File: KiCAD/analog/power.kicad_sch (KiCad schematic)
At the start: 31 parts, among them J33 Screw_Terminal_01x02, J34 Screw_Terminal_01x02, J5 Screw_Terminal_01x02, K5 G6RL-1-DC12, U13 MCP1700x-330xxTO, U6 LM2940CT-5.0, U7 LT1054, U8 LM2940CT-12, U9 LT1054

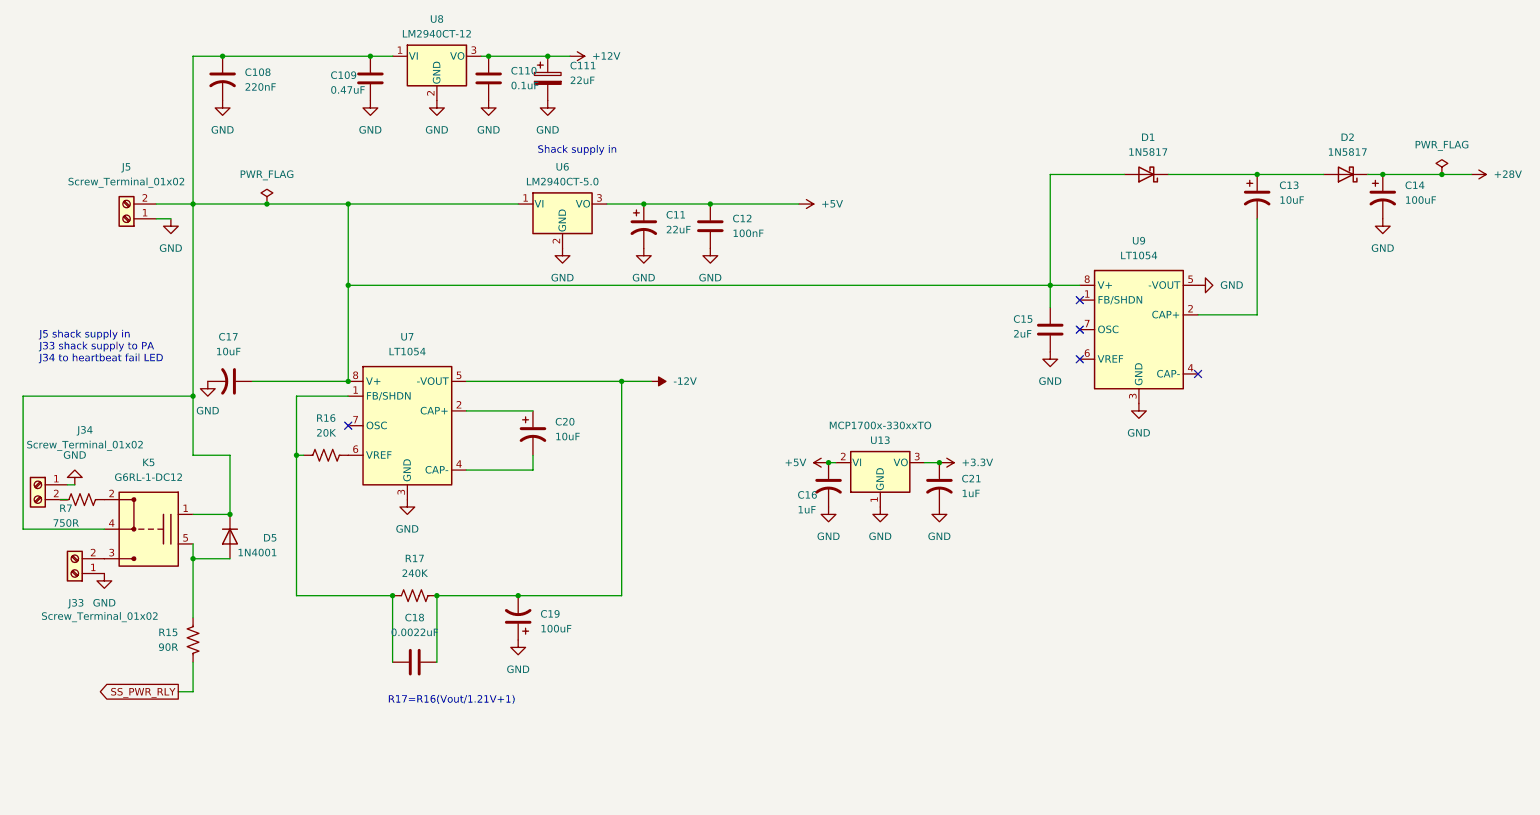
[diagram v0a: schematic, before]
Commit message: revD: drop 10m, convert LPF to DPDT G6K throughout, retire +28V rail
Output LPF:
- 10m bank removed (K8/K1-equivalent, L15/L16/L17, CF14-CF25 and
  parallel-cap combos, R4 original). 10m to be handled via main rig.
- All 4 remaining bands now use a single xmitter:Relay_G6K DPDT per
  bank (K1=15m, K2=17m, K3=20m, K4=40m). Pole 1 switches output,
  Pole 2 switches input. Half the relay count vs the old SPST pair.
- Coil chain per bank: pin1=+12V, pin8=RLY_xx_DRIVE via 2N7000
  (Q5/Q8/Q1/Q10 for 15/17/20/40) with 1N4148 flyback (D7/D8/D9/D11).
- Swamp resistors (R2-R9, 2 per bank) placed on relay pin 7 (NC) so
  they only load the LPF when the bank is unselected -- removes
  active-path insertion loss.
- Legacy screw terminals J16/J25/J26/J27/J29 and +28V coil feed
  deleted. Umbilical now carries +12V on J2 pin 8.

Analog:
- LT1054 +28V voltage doubler (U9) and its support caps/diodes
  removed. +28V net purged from every sheet.
- +12V (LM2940CT-12 U8) now feeds the LPF coil supply via J2 pin 8.
- LT1054 -12V inverter (U7) retained for LM7171 negative rail.
- +12V current budget: ~75-100 mA worst case (op-amp rails + one
  G6K coil active) against 1 A LDO capacity.

Co-Authored-By: Claude Opus 4.7 <noreply@anthropic.com>
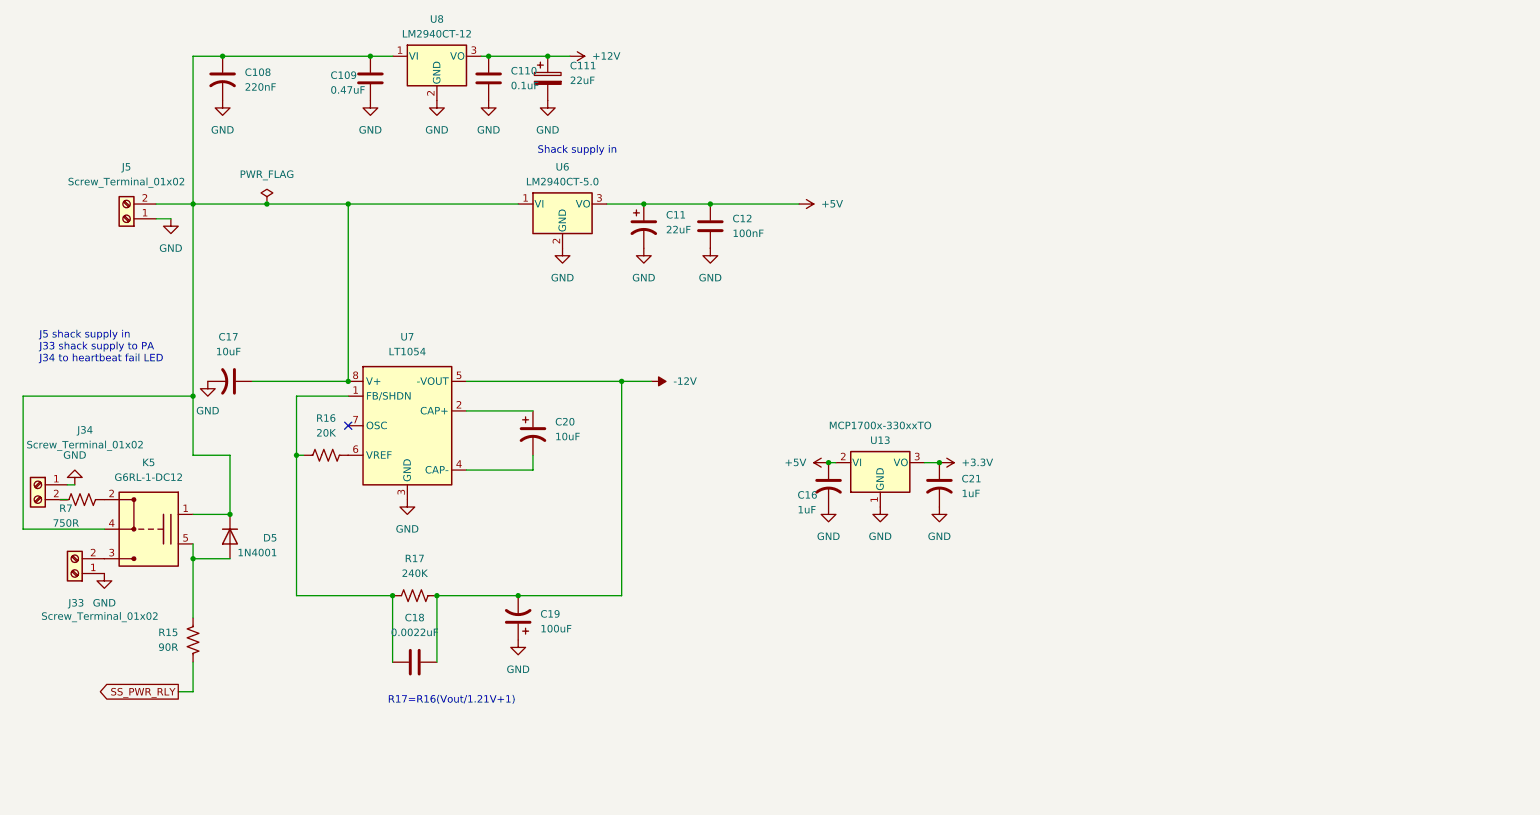
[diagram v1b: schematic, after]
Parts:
- removed C13: 10uF, Capacitor_THT:CP_Radial_D5.0mm_P2.00mm, symbol Device:C_Polarized_US
- removed C14: 100uF, Capacitor_THT:CP_Radial_D8.0mm_P5.00mm, symbol Device:C_Polarized_US
- removed C15: 2uF, Capacitor_THT:C_Rect_L7.2mm_W4.5mm_P5.00mm, symbol Device:C
- removed D1, D2: 1N5817, Diode_THT:D_DO-41_SOD81_P10.16mm_Horizontal, symbol Diode:1N5817
- removed U9: LT1054, Package_DIP:DIP-8_W7.62mm, symbol Regulator_SwitchedCapacitor:LT1054
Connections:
- no-connect marks 5 -> 1

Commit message: revD analog: shack supply input protection -- fuse + Schottky
- Add 3A slow-blow blade fuse on +13.8V input at J5. Catches
  downstream shorts (IRF510 drain-source failure, trace short)
  before the drain-feed trace, T203 bifilar, or shack-supply wiring
  smokes. Blows well below the shack supply's own ~25A protection.
- Add reverse-polarity Schottky in series on the input path (1N5822
  or SB540 class).
- xmitter library additions:
    * symbol:   Fuse_Blade_3568 (copied from stock Device:Fuse,
                pre-linked to the footprint below, default value
                Fuse_3A_SlowBlow)
    * footprint: Fuse_Blade_Keystone_3568 (Keystone 3568 PCB-mount
                 ATM mini blade fuse holder; 16 x 6.73 mm body, 4
                 x 1.6 mm NPTH on 9.92 x 3.40 mm 2x2 pattern)
- Documentation: Keystone 3568 datasheet (3568 holder.pdf)

Co-Authored-By: Claude Opus 4.7 <noreply@anthropic.com>
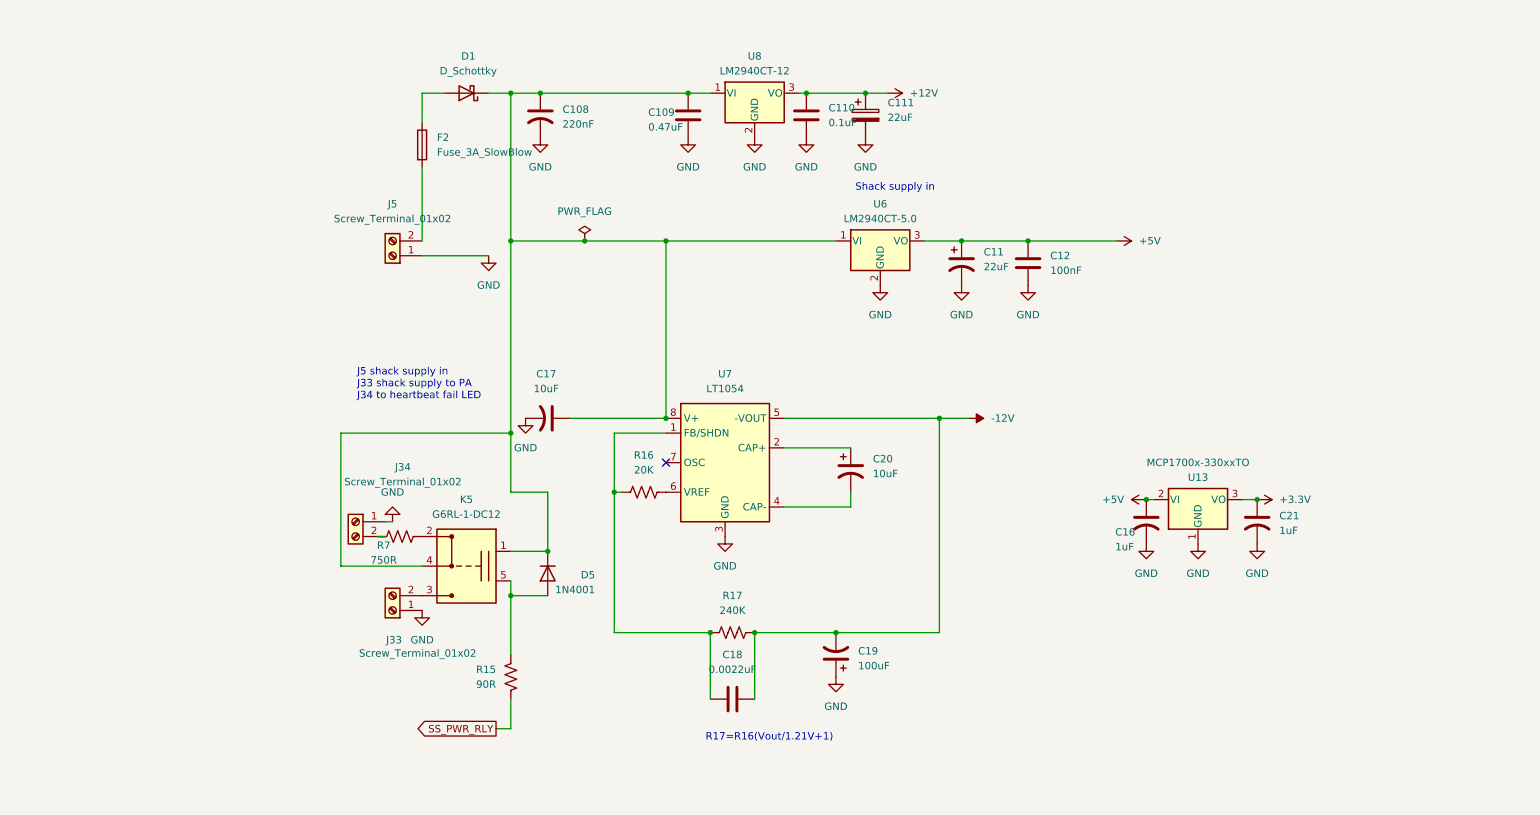
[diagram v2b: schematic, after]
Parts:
- added D1: D_Schottky, symbol Device:D_Schottky
- added F2: Fuse_3A_SlowBlow, xmitter:Fuse_Blade_Keystone_3568, symbol xmitter:Fuse_Blade_3568
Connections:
- net at C108.1, C109.1, C17.1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: now also D1.1 (K); no longer J5.2 (Pin_2)
- new net: D1.2 (A), F2.1
- new net: F2.2, J5.2 (Pin_2)
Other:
- moved on the sheet: C108, C109, C11, C110, C111, C12, C16, C17, C18, C19, C20, C21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

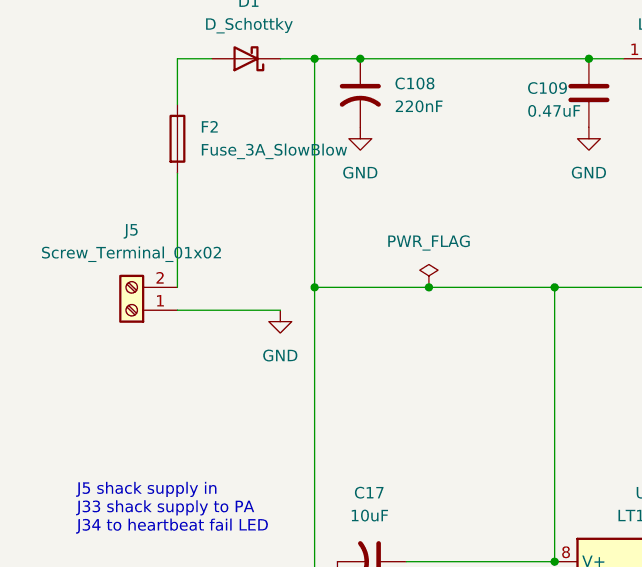
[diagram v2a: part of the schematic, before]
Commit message: revD: ss_pa Option C 5V rail + analog SW1 THT + R/C footprints + doc refresh
ss_pa Option C: swap U13 to LM2936Z-5.0 (full +5V logic rail), re-size
R10 10K->6.8K to preserve ~0.3V fault trip at new rail, drop +3.3V net
entirely. Fixes the previously-dead +5V bus that had no source.

Analog SW1 (Si5351 bringup DPDT): swap SMD footprint for
Button_Switch_THT:SW_CK_JS202011CQN_DPDT_Straight. Verified pin-numbering
convention (pin 1 above pin 6 in THT) matches user's intended DPST
wiring; both SDA/SCL break together.

Analog: assign missing footprints to R3/R4/R5/R8/R9 (DIN0207 axial) and
C4/C5/C6/C7/C8 (disc ceramic 5mm). Add xmitter:DIP-14_W7.62mm.kicad_mod
and 74HCT125 symbol to the xmitter library.

Documentation: Rev D handoff doc updated with M1-M8 fix status, Option C
notes, I2C bus voltage architecture, 74HCT125 SPI shifter, FAULT_N
divider details, and Metro-no-footprint note. Supporting docs updated:
i2c_bus.md full rewrite for 5V HV bus + STEMMA reroute, revD_interconnect
board inventory refresh, status banners on ss_pa.md / Master_Description /
cw_envelope_keyer / front_panel_interface pointing to handoff doc for
items beyond their last-current date.

Co-Authored-By: Claude Opus 4.7 <noreply@anthropic.com>
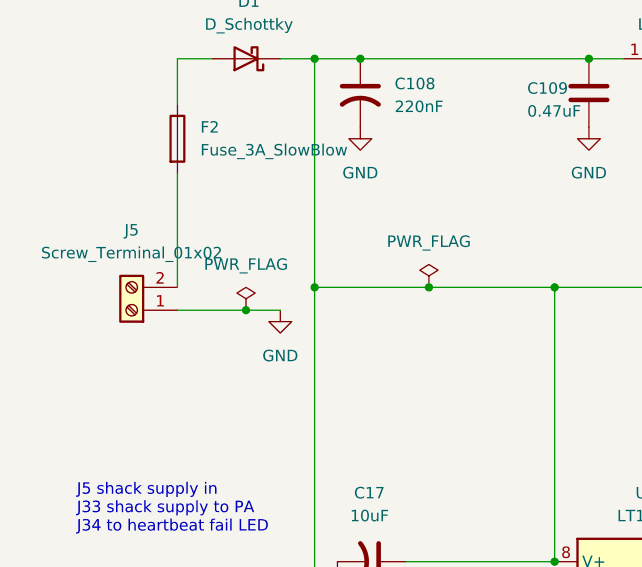
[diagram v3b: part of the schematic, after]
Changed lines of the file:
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@@
 	)
 	(junction
+		(at 90.17 69.85)
+		(diameter 0)
+		(color 0 0 0 0)
+	)
+	(junction
 		(at 128.27 41.91)
 		(diameter 0)
@@
 	(wire
 		(pts
+			(xy 90.17 69.85) (xy 93.98 69.85)
+		)
+		(stroke
+			(width 0)
+			(type default)
+		)
+	)
+	(wire
+		(pts
 			(xy 171.45 97.79) (xy 171.45 134.62)
 		)
@@
 	(wire
 		(pts
-			(xy 82.55 69.85) (xy 93.98 69.85)
+			(xy 82.55 69.85) (xy 90.17 69.85)
 		)
 		(stroke
@@
 					(unit 1)
 				)
+			)
+		)
+	)
+	(symbol
+		(lib_id "power:PWR_FLAG")
+		(at 90.17 69.85 0)
+		(unit 1)
+		(body_style 1)
+		(exclude_from_sim no)
+		(in_bom yes)
+		(on_board yes)
+		(in_pos_files yes)
+		(dnp no)
+		(fields_autoplaced yes)
+		(property "Reference" "#FLG02"
+			(at 90.17 67.945 0)
+			(hide yes)
+			(show_name no)
+			(do_not_autoplace no)
+			(effects
+				(font
+					(size 1.27 1.27)
+				)
+			)
+		)
+		(property "Value" "PWR_FLAG"
+			(at 90.17 64.77 0)
+			(show_name no)
+			(do_not_autoplace no)
+			(effects
+				(font
+					(size 1.27 1.27)
+				)
+			)
+		)
+		(property "Footprint" ""
+			(at 90.17 69.85 0)
+			(hide yes)
+			(show_name no)
+			(do_not_autoplace no)
+			(effects
+				(font
+					(size 1.27 1.27)
+				)
+			)
+		)
+		(property "Datasheet" ""
+			(at 90.17 69.85 0)
+			(hide yes)
+			(show_name no)
+			(do_not_autoplace no)
+			(effects
+				(font
+					(size 1.27 1.27)
+				)
+			)
+		)
+		(property "Description" "Special symbol for telling ERC where power comes from"
+			(at 90.17 69.85 0)
+			(hide yes)
+			(show_name no)
+			(do_not_autoplace no)
+			(effects
+				(font
+					(size 1.27 1.27)
+				)
+			)
+		)
+		(pin "1"
+		)
+		(instances
+			(project "analog"
+				(path "/d3de40b8-856b-4fbd-829c-f45ffcd55742/9d33972e-4f39-4043-b71d-952850d73035"
+					(reference "#FLG02")
+					(unit 1)
+				)

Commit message: revD analog: DGFET op-amp offset-mute topology + doc updates
Retire the Q11/Q12 PNP KeyUp mute path on the DGFET keyer G2 (sim showed
only ~2.6:1 on/off ratio with G1 biased above V_TO). Replace with an
LM7171 (U10) non-inverting op-amp wired as DC offset:
  V_G2 = V_DAC * (1 + R20/R23) - V_ref * (R20/R23)
with V_ref ~5.05V (1N4733A Zener D2, R24 1K bias, R25 1K / R32 100K
summing divider) and R20=6.2K / R23=10K (G=0.62). DAC=0 drives G2 to
-3.1V (fully cuts off the 40673, sim-verified 12pA leakage, ~10^9 on/off
ratio); DAC=5V drives G2 to +5V (matches prior keyed operating point).
KEY_UP net eliminated -- mute is intrinsic to the signal path, firmware
controls RF enable/disable solely via what it writes to the MCP4921
envelope channel.

Includes new test.kicad_sch sheet carrying the U10/R20-R32 subcircuit.

Doc updates: CLAUDE.md DGFET section rewritten; handoff doc gets a new
"DGFET keyer mute topology" section explaining retirement reason and
new transfer function; Master_Description Sec 2 and SPI-bus section
updated; revD_interconnect G2 amplitude-control block updated;
control_board_functional_blocks.md gets a prominent retirement banner
pointing at the current scheme.

Co-Authored-By: Claude Opus 4.7 <noreply@anthropic.com>
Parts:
- R17: value 240K -> 220K
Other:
- note added: "Fault LED"
- note added: "SS PA Power"
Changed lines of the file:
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@@
+		)
+	)
+	(text "SS PA Power"
+		(exclude_from_sim no)
+		(at 66.294 130.302 0)
+		(effects
+			(font
+				(size 1.27 1.27)
+			)
+		)
+	)
+	(text "Fault LED"
+		(exclude_from_sim no)
+		(at 61.722 117.348 0)
+		(effects
+			(font
+				(size 1.27 1.27)
+			)
 		)
 	)
@@
 			)
 		)
-		(property "Value" "240K"
+		(property "Value" "220K"
 			(at 135.89 130.81 90)
 			(show_name no)
